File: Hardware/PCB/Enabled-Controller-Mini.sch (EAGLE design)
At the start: 9 parts

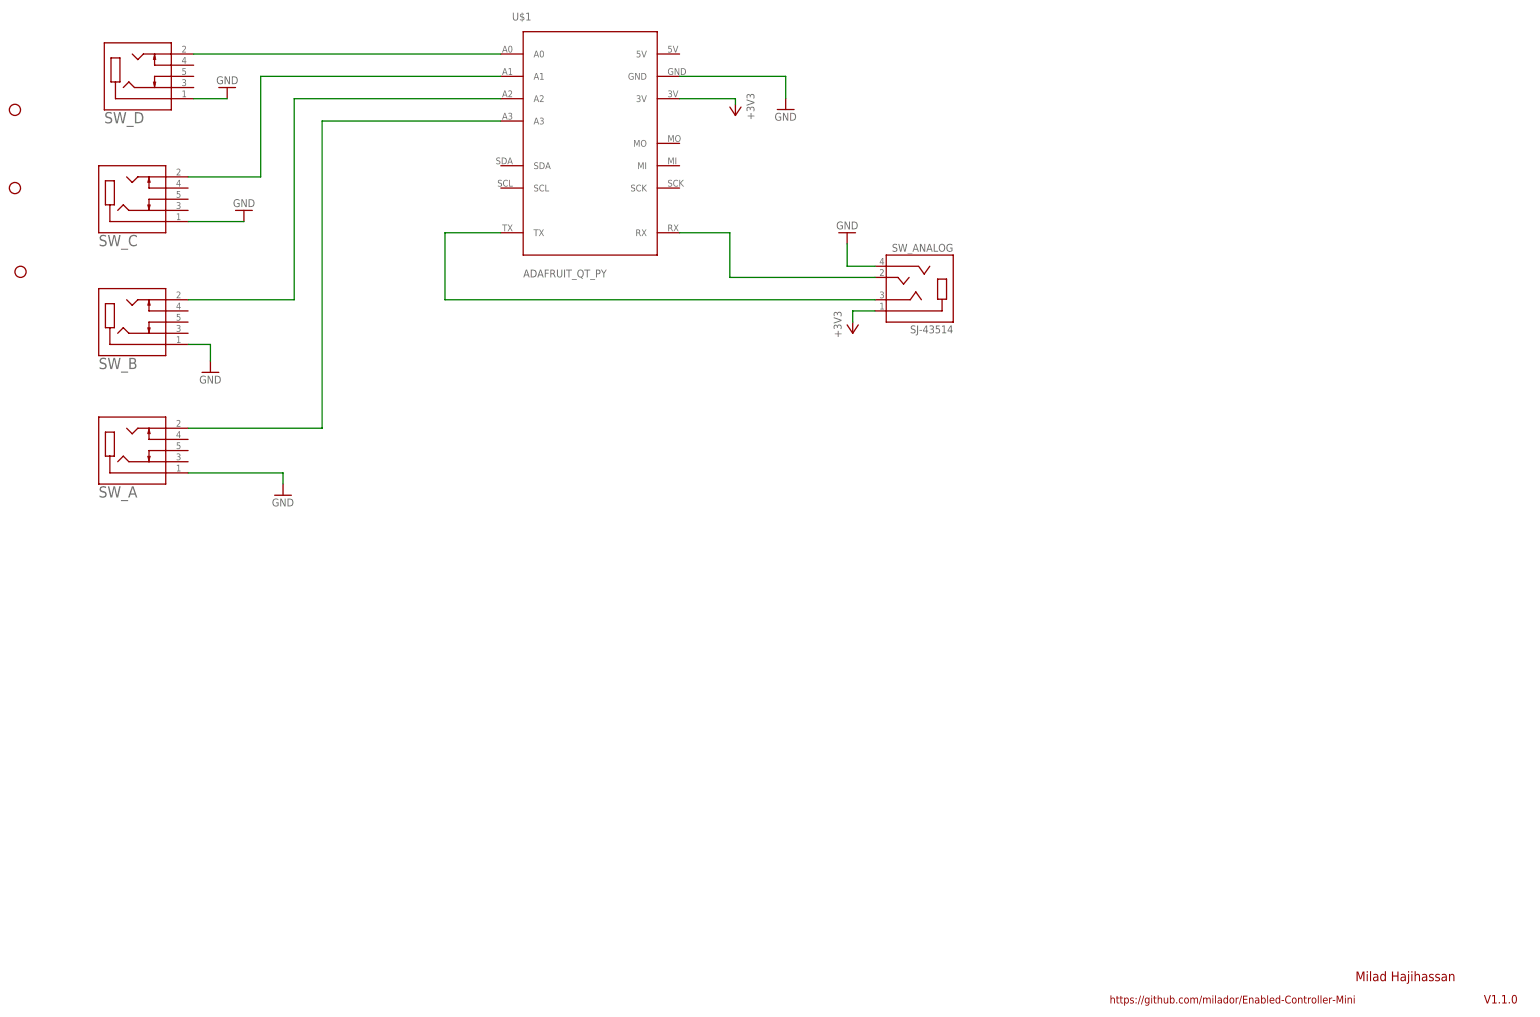
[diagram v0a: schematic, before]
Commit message: Reversed PCB design file
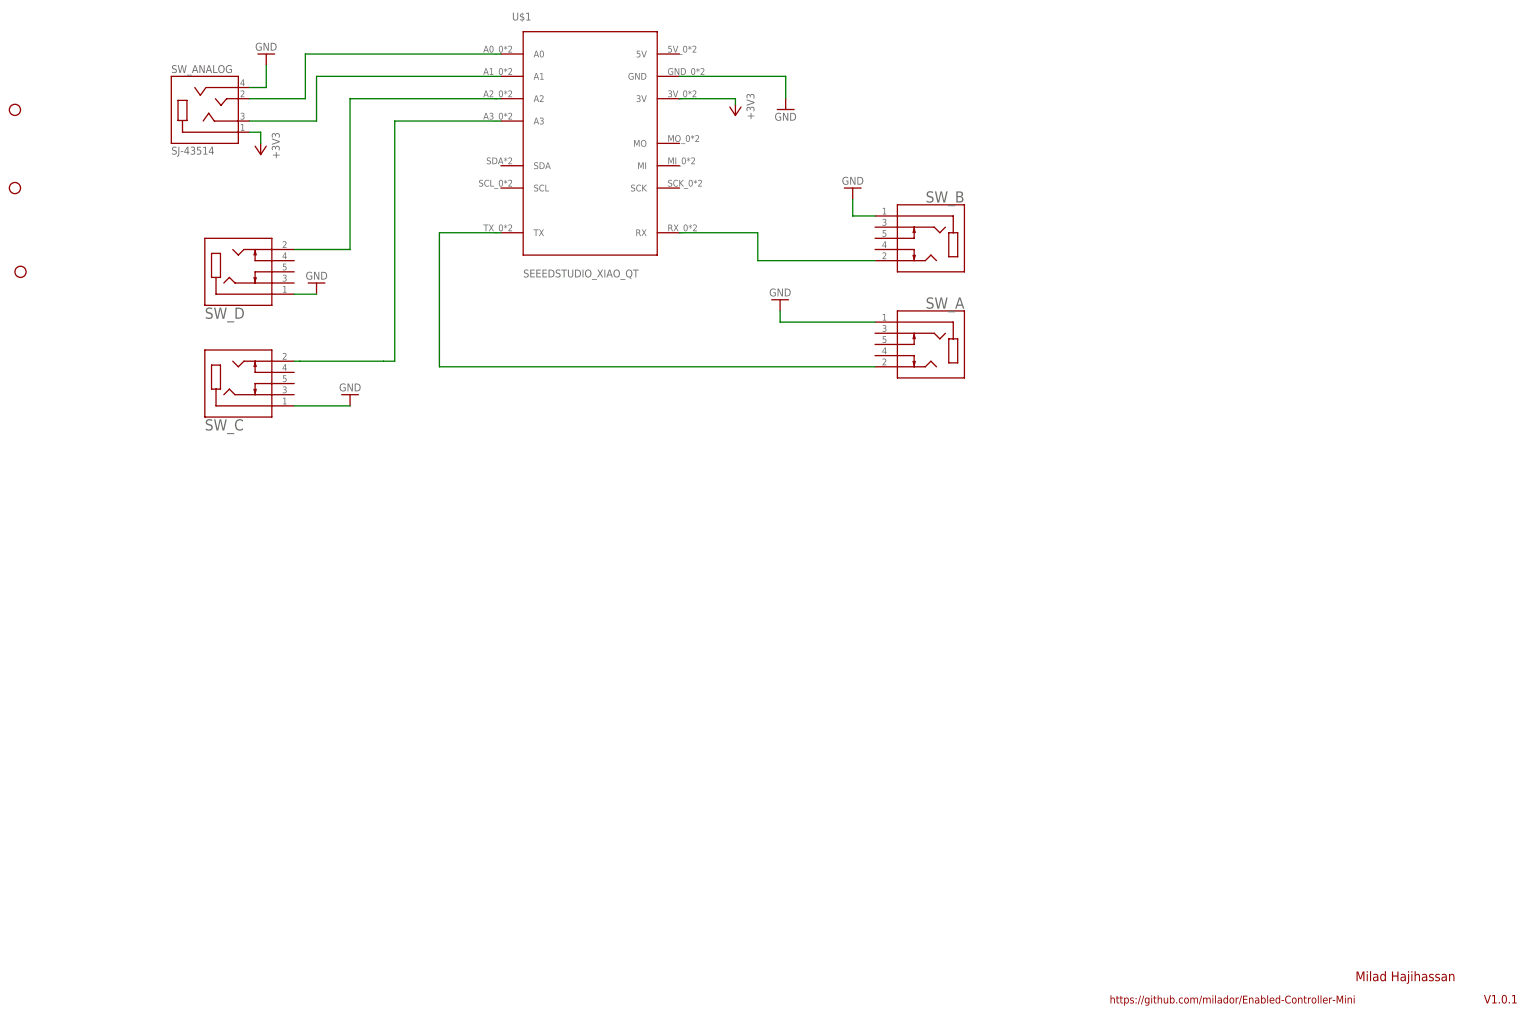
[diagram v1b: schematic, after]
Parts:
- U$1: value ADAFRUIT_QT_PY -> SEEEDSTUDIO_XIAO_QT; device MMC Eagle:ADAFRUIT_QT_PY -> MMC Eagle:SEEEDSTUDIO_XIAO_QT
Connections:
- removed net N$3: SW_D.2, U$1.A0
- new net N$11: SW_D.2, U$1.A2
- net N$1: now also U$1.RX; no longer U$1.A2
- net N$2: now also U$1.TX; no longer U$1.A3
- net N$4: now also U$1.A0; no longer U$1.RX
- net N$5: now also U$1.A3; no longer U$1.A1
- net N$8: now also U$1.A1; no longer U$1.TX
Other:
- note added: "V1.0.1"
- note removed: "V1.1.0"
- moved on the sheet: SW_A, SW_ANALOG, SW_B, SW_C, SW_D

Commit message: Updated PCB design files : SWITCH GPIO's changed to A0,A1,A2,A3
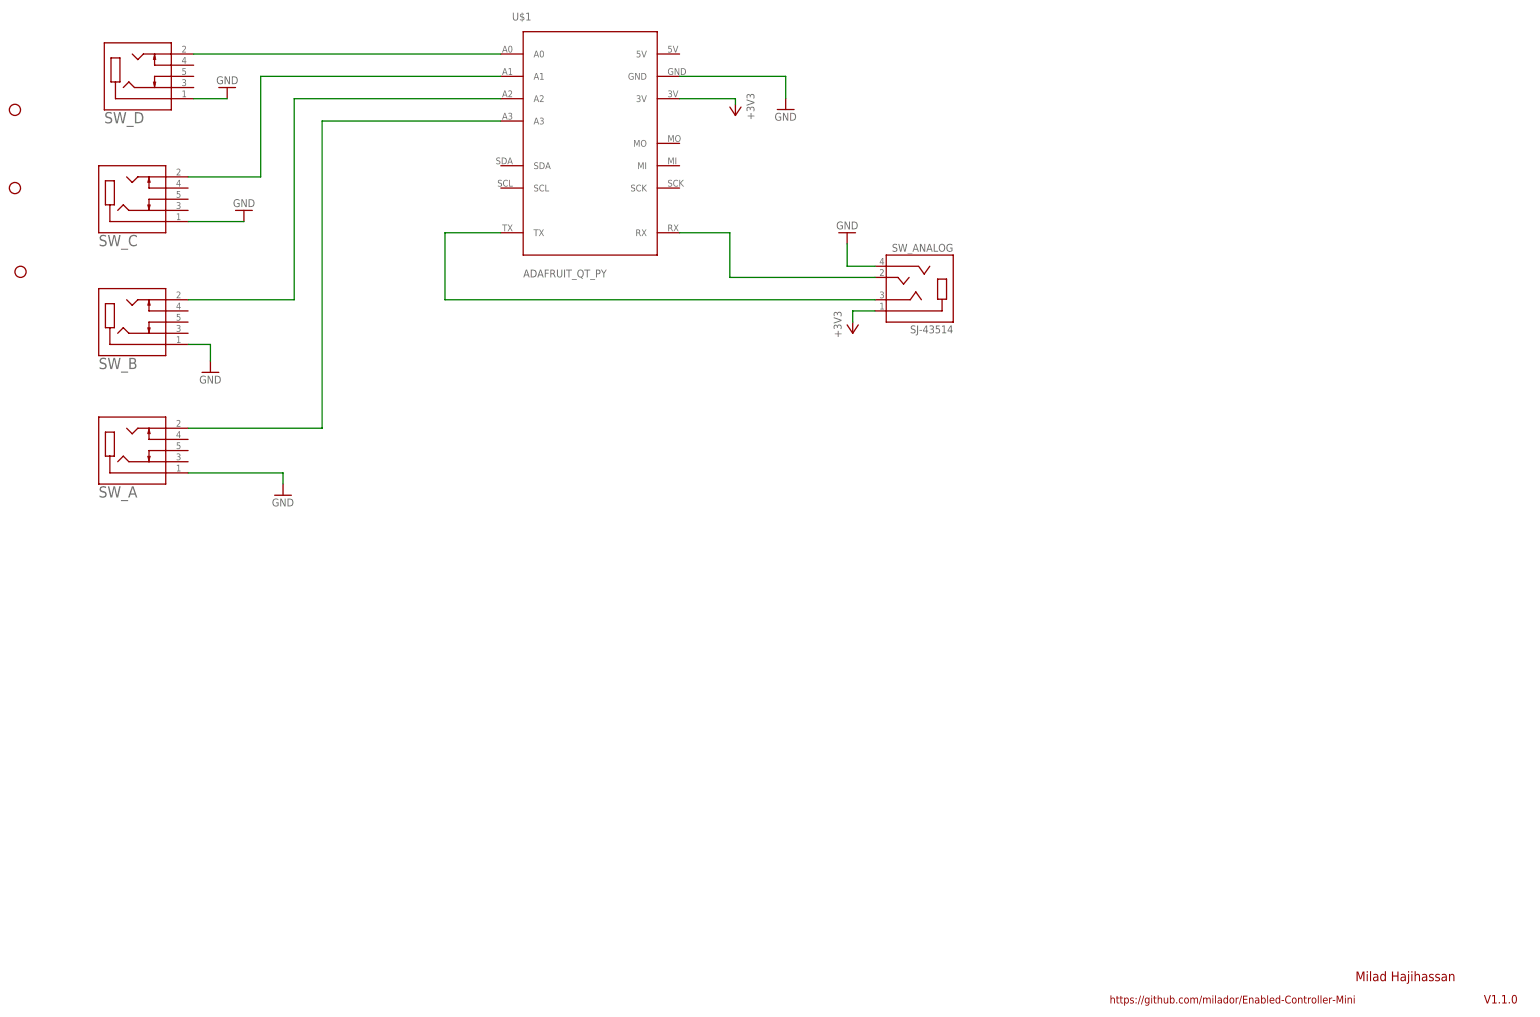
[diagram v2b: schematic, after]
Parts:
- U$1: value SEEEDSTUDIO_XIAO_QT -> ADAFRUIT_QT_PY; device MMC Eagle:SEEEDSTUDIO_XIAO_QT -> MMC Eagle:ADAFRUIT_QT_PY
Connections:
- removed net N$11: SW_D.2, U$1.A2
- new net N$3: SW_D.2, U$1.A0
- net N$1: now also U$1.A2; no longer U$1.RX
- net N$2: now also U$1.A3; no longer U$1.TX
- net N$4: now also U$1.RX; no longer U$1.A0
- net N$5: now also U$1.A1; no longer U$1.A3
- net N$8: now also U$1.TX; no longer U$1.A1
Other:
- note added: "V1.1.0"
- note removed: "V1.0.1"
- moved on the sheet: SW_A, SW_ANALOG, SW_B, SW_C, SW_D
